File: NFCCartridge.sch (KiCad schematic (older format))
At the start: 3 parts, among them J1 Cartridge Connector, U1 W25Q128

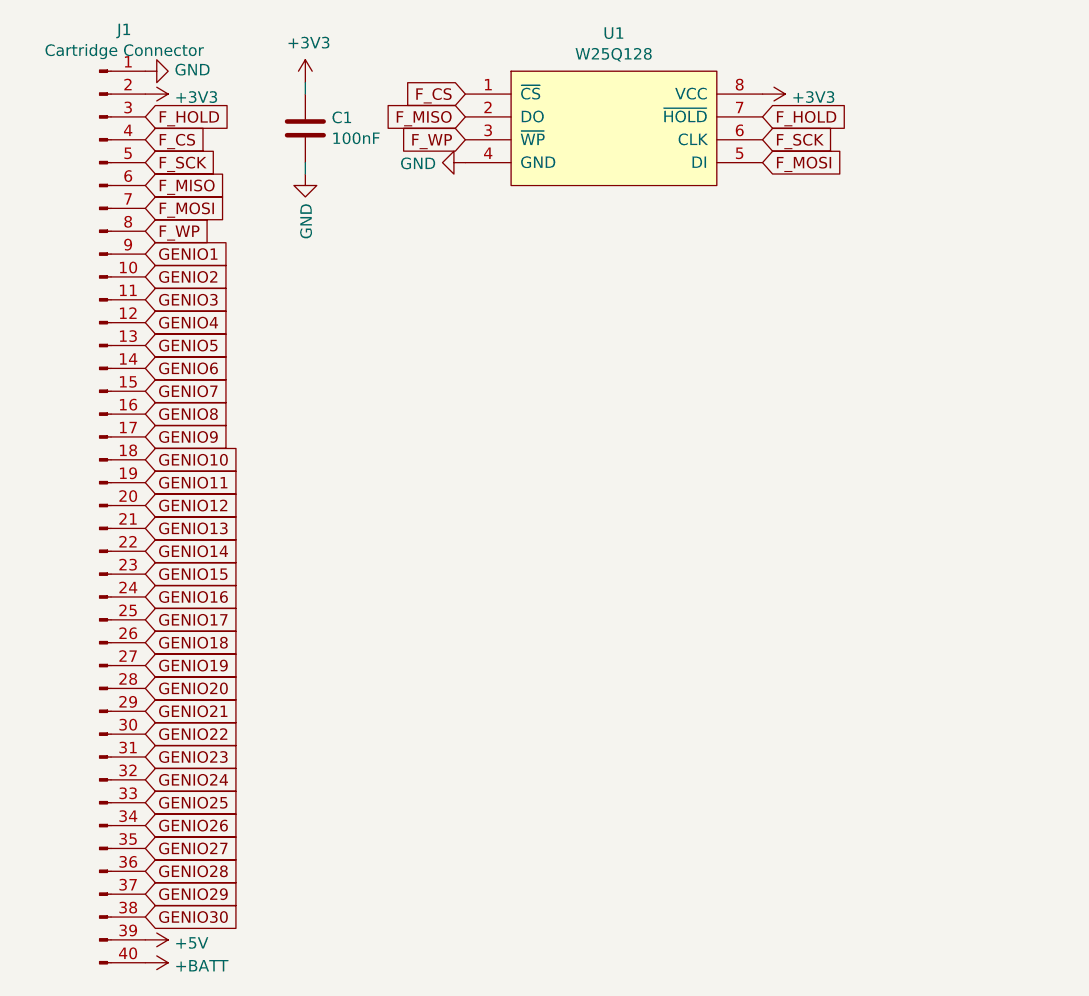
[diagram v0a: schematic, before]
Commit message: First design of the NFC Cartridge
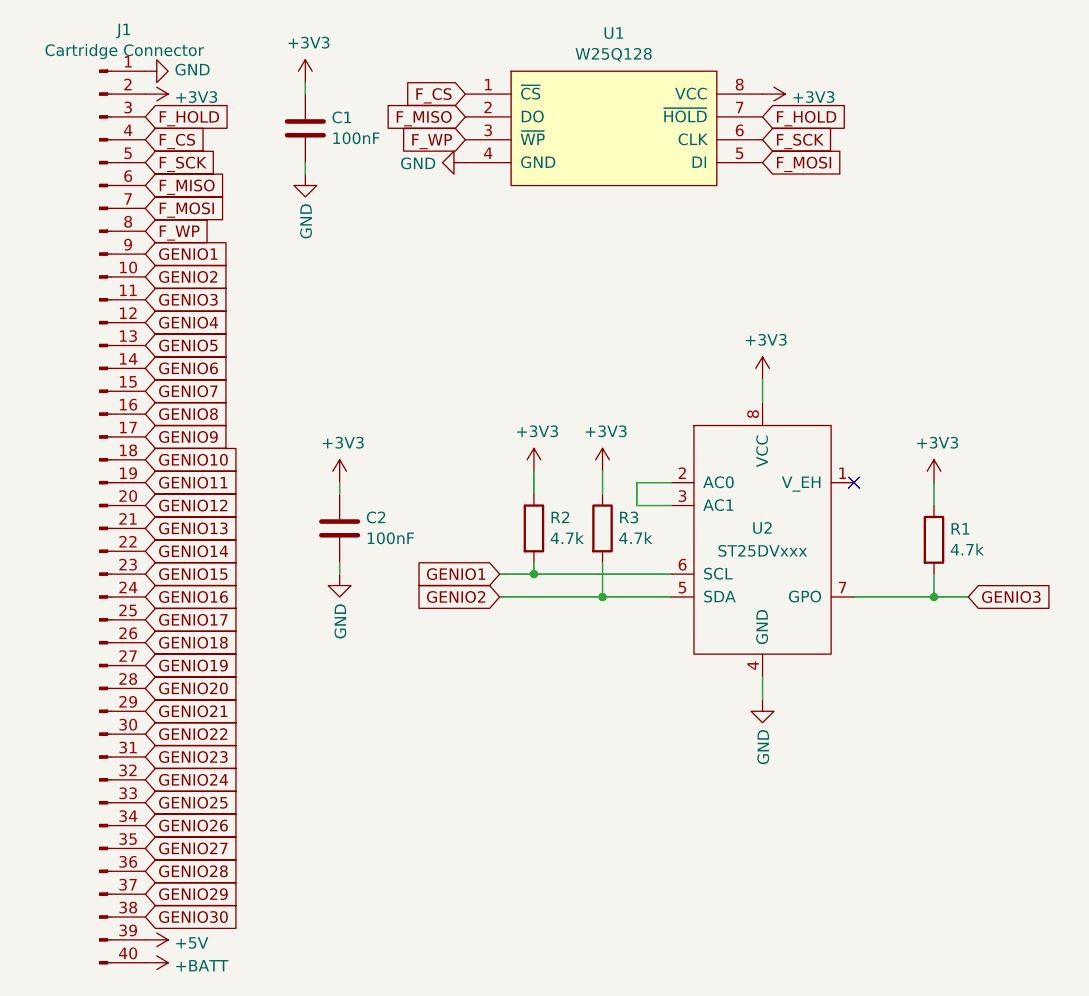
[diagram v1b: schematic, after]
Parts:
- added C2: 100nF, Capacitors_SMD:C_0805_HandSoldering, symbol device:C
- added R1, R2, R3: 4.7k, Resistors_SMD:R_0805_HandSoldering, symbol device:R
- added U2: ST25DVxxx, Housings_SOIC:SOIC-8_3.9x4.9mm_Pitch1.27mm, symbol SuperconCartridge:ST25DVxxx
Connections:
- net +3V3: now also C2.1, R1.1, R2.1, R3.1, U2.8 (VCC)
- net GENIO1: now also R2.2, U2.6 (SCL)
- net GENIO2: now also R3.2, U2.5 (SDA)
- net GENIO3: now also R1.2, U2.7 (GPO)
- net GND: now also C2.2, U2.4 (GND)
- new net: U2.2 (AC0), U2.3 (AC1)
- no-connect marks 0 -> 1
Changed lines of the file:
@@
-EESchema Schematic File Version 4
-EELAYER 29 0
+EESchema Schematic File Version 5
+EELAYER 30 0
 EELAYER END
 $Descr A4 11693 8268
 encoding utf-8
 Sheet 1 1
-Title "Supercon 2019 Badge Cartridge Template"
+Title "NFC Cartridge for Supercon 2019 Badge"
 Date ""
 Rev ""
-Comp "Template designed by: @thomasflummer"
+Comp "Designed by: @thomasflummer"
 Comment1 "License: CC-BY-SA"
 Comment2 ""
 Comment3 ""
 Comment4 ""
+Comment5 ""
+Comment6 ""
+Comment7 ""
+Comment8 ""
+Comment9 ""
 $EndDescr
 $Comp
@@
 Wire Wire Line
 	2000 1500 2000 1550
+$Comp
+L SuperconCartridge:ST25DVxxx U2
+U 1 1 5DB74DA0
+P 4000 3150
+F 0 "U2" H 4000 3200 50  0000 C CNN
+F 1 "ST25DVxxx" H 4000 3100 50  0000 C CNN
+F 2 "Housings_SOIC:SOIC-8_3.9x4.9mm_Pitch1.27mm" H 4000 3150 50  0001 C CNN
+F 3 "" H 4000 3150 50  0001 C CNN
+	1    4000 3150
+	1    0    0    -1
+$EndComp
+Wire Wire Line
+	3600 2900 3450 2900
+Wire Wire Line
+	3450 2900 3450 3000
+Wire Wire Line
+	3450 3000 3600 3000
+$Comp
+L power:+3V3 #PWR09
+U 1 1 5DB7773E
+P 4000 2450
+F 0 "#PWR09" H 4000 2300 50  0001 C CNN
+F 1 "+3V3" H 4015 2623 50  0000 C CNN
+F 2 "" H 4000 2450 50  0001 C CNN
+F 3 "" H 4000 2450 50  0001 C CNN
+	1    4000 2450
+	1    0    0    -1
+$EndComp
+$Comp
+L power:GND #PWR013
+U 1 1 5DB77C8D
+P 4000 3850
+F 0 "#PWR013" H 4000 3600 50  0001 C CNN
+F 1 "GND" V 4005 3722 50  0000 R CNN
+F 2 "" H 4000 3850 50  0001 C CNN
+F 3 "" H 4000 3850 50  0001 C CNN
+	1    4000 3850
+	1    0    0    -1
+$EndComp
+Wire Wire Line
+	4000 2550 4000 2450
+Wire Wire Line
+	4000 3850 4000 3750
+$Comp
+L device:R R1
+U 1 1 5DB77FAC
+P 4750 3150
+F 0 "R1" H 4820 3196 50  0000 L CNN
+F 1 "4.7k" H 4820 3105 50  0000 L CNN
+F 2 "Resistors_SMD:R_0805_HandSoldering" V 4680 3150 50  0001 C CNN
+F 3 "~" H 4750 3150 50  0001 C CNN
+	1    4750 3150
+	1    0    0    -1
+$EndComp
+$Comp
+L power:+3V3 #PWR010
+U 1 1 5DB79035
+P 4750 2900
+F 0 "#PWR010" H 4750 2750 50  0001 C CNN
+F 1 "+3V3" H 4765 3073 50  0000 C CNN
+F 2 "" H 4750 2900 50  0001 C CNN
+F 3 "" H 4750 2900 50  0001 C CNN
+	1    4750 2900
+	1    0    0    -1
+$EndComp
+Text GLabel 2850 3300 0    50   Input ~ 0
+GENIO1
+Text GLabel 2850 3400 0    50   Input ~ 0
+GENIO2
+Text GLabel 4900 3400 2    50   Input ~ 0
+GENIO3
+Wire Wire Line
+	4750 2900 4750 3000
+Wire Wire Line
+	4900 3400 4750 3400
+Wire Wire Line
+	4750 3300 4750 3400
+Connection ~ 4750 3400
+Wire Wire Line
+	4750 3400 4400 3400
+NoConn ~ 4400 2900
+Wire Wire Line
+	2150 2900 2150 2950
+Wire Wire Line
+	2150 3250 2150 3300
+$Comp
+L device:C C2
+U 1 1 5DB79968
+P 2150 3100
+F 0 "C2" H 2265 3146 50  0000 L CNN
+F 1 "100nF" H 2265 3055 50  0000 L CNN
+F 2 "Capacitors_SMD:C_0805_HandSoldering" H 2188 2950 50  0001 C CNN
+F 3 "~" H 2150 3100 50  0001 C CNN
+	1    2150 3100
+	1    0    0    -1
+$EndComp
+$Comp
+L power:+3V3 #PWR011
+U 1 1 5DB79979
+P 2150 2900
+F 0 "#PWR011" H 2150 2750 50  0001 C CNN
+F 1 "+3V3" H 2165 3073 50  0000 C CNN
+F 2 "" H 2150 2900 50  0001 C CNN
+F 3 "" H 2150 2900 50  0001 C CNN
+	1    2150 2900
+	1    0    0    -1
+$EndComp
+$Comp
+L power:GND #PWR012
+U 1 1 5DB79987
+P 2150 3300
+F 0 "#PWR012" H 2150 3050 50  0001 C CNN
+F 1 "GND" V 2155 3172 50  0000 R CNN
+F 2 "" H 2150 3300 50  0001 C CNN
+F 3 "" H 2150 3300 50  0001 C CNN
+	1    2150 3300
+	1    0    0    -1
+$EndComp
+$Comp
+L device:R R3
+U 1 1 5DB7E4DC
+P 3300 3100
+F 0 "R3" H 3370 3146 50  0000 L CNN
+F 1 "4.7k" H 3370 3055 50  0000 L CNN
+F 2 "Resistors_SMD:R_0805_HandSoldering" V 3230 3100 50  0001 C CNN
+F 3 "~" H 3300 3100 50  0001 C CNN
+	1    3300 3100
+	1    0    0    -1
+$EndComp
+$Comp
+L power:+3V3 #PWR015
+U 1 1 5DB7E4ED
+P 3300 2850
+F 0 "#PWR015" H 3300 2700 50  0001 C CNN
+F 1 "+3V3" H 3315 3023 50  0000 C CNN
+F 2 "" H 3300 2850 50  0001 C CNN
+F 3 "" H 3300 2850 50  0001 C CNN
+	1    3300 2850
+	1    0    0    -1
+$EndComp
+Wire Wire Line
+	3300 2850 3300 2950
+Wire Wire Line
+	3000 2850 3000 2950
+$Comp
+L device:R R2
+U 1 1 5DB8132B
+P 3000 3100
+F 0 "R2" H 3070 3146 50  0000 L CNN
+F 1 "4.7k" H 3070 3055 50  0000 L CNN
+F 2 "Resistors_SMD:R_0805_HandSoldering" V 2930 3100 50  0001 C CNN
+F 3 "~" H 3000 3100 50  0001 C CNN
+	1    3000 3100
+	1    0    0    -1
+$EndComp
+$Comp
+L power:+3V3 #PWR014
+U 1 1 5DB8133C
+P 3000 2850
+F 0 "#PWR014" H 3000 2700 50  0001 C CNN
+F 1 "+3V3" H 3015 3023 50  0000 C CNN
+F 2 "" H 3000 2850 50  0001 C CNN
+F 3 "" H 3000 2850 50  0001 C CNN
+	1    3000 2850
+	1    0    0    -1
+$EndComp
+Wire Wire Line
+	2850 3300 3000 3300
+Wire Wire Line
+	2850 3400 3300 3400
+Wire Wire Line
+	3300 3250 3300 3400
+Connection ~ 3300 3400
+Wire Wire Line
+	3300 3400 3600 3400
+Wire Wire Line
+	3000 3250 3000 3300
+Connection ~ 3000 3300
+Wire Wire Line
+	3000 3300 3600 3300
 $EndSCHEMATC
